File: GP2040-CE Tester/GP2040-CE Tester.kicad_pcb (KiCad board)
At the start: 2 copper layers, 102 x 54 mm, 69 parts, among them J1 USB_B, J2 USB_A, J3 USB_A, U1 RP2040, U2 SIT2018BE-S8-33N-12.000000G, U3 W25Q128JVS, U4 NCP1117-3.3_SOT223, U5 TUSB4041IPAPR, U6 PTMUXHS221NKGR, U7 ATmega2560-16A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

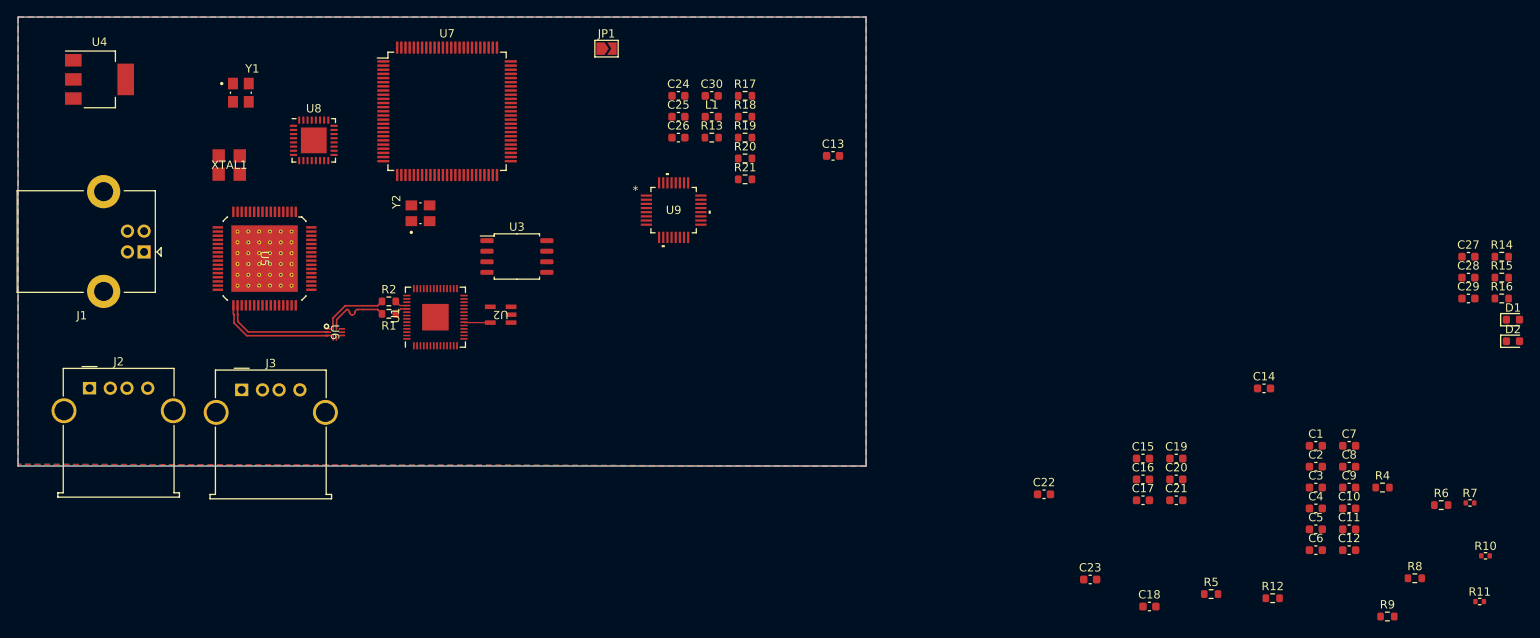
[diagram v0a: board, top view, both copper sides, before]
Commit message: adding most of the components, and schematic connections
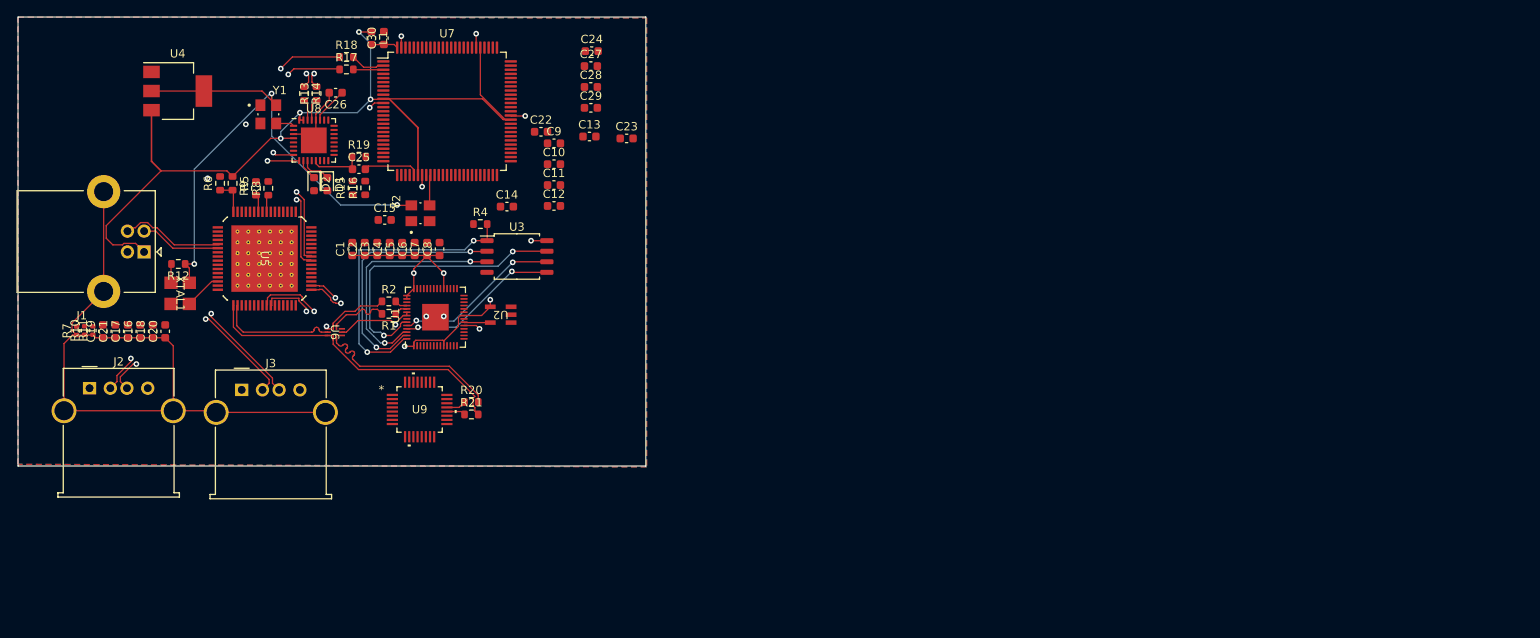
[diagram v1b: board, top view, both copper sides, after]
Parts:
- removed JP1: Jumper_2_Open, Jumper:SolderJumper-2_P1.3mm_Open_TrianglePad1.0x1.5mm
- moved R10 170.7 mm to (99.0, 76.7), turned to 90 degrees
- moved R11 170.0 mm to (100.0, 76.7), turned to 90 degrees
- moved R7 168.9 mm to (98.0, 76.7), turned to 90 degrees
- moved R6 151.9 mm to (115.3, 59.0), turned to 90 degrees
- moved R8 145.7 mm to (121.1, 59.6), turned to 90 degrees
- moved R9 145.5 mm to (119.6, 59.6), turned to 90 degrees
- moved D2 145.4 mm to (126.6, 59.1), turned to -90 degrees
- moved R14 145.4 mm to (125.4, 48.2), turned to -90 degrees
- moved D1 143.5 mm to (128.2, 59.1), turned to -90 degrees
- moved R15 138.6 mm to (131.2, 59.6), turned to 90 degrees
- moved R12 137.6 mm to (110.3, 68.7), turned to 180 degrees
- moved R16 137.3 mm to (132.8, 59.6), turned to 90 degrees
- moved C19 130.0 mm to (101.2, 76.8), turned to 90 degrees
- moved C21 129.2 mm to (102.7, 76.8), turned to 90 degrees
- moved R5 127.6 mm to (116.8, 59.0), turned to -90 degrees
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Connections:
- net /Sheetname: Embeded RP2040/clock renamed /Sheetname: Embeded RP2040/CLK
- net Net-(J1-D+) renamed /Sheetname: USB Hub/UPSD+
- net Net-(J1-D-) renamed /Sheetname: USB Hub/UPSD-
- net Net-(U1-USB_DM) renamed /Sheetname: Embeded RP2040/LD-
- net Net-(U1-USB_DP) renamed /Sheetname: Embeded RP2040/LD+
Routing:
- net +3.3V: track 0.00 -> 164.2 mm, vias 0 -> 9
- net +5V: track 0.00 -> 106.8 mm, vias 0 -> 4
- net Earth: track 0.00 -> 80.6 mm
- net /Sheetname: USB Hub/USB_4_D-: track 0.00 -> 46.6 mm, vias 0 -> 2
- net /Sheetname: USB Hub/USB_4_D+: track 0.00 -> 46.4 mm, vias 0 -> 2
- net /Sheetname: Mega2560/MEGA_USB_D+: track 0.00 -> 38.4 mm, vias 0 -> 2
- net /Sheetname: Mega2560/MEGA_USB_D-: track 0.00 -> 38.4 mm, vias 0 -> 2
- net /Sheetname: USB Hub/USB_3_D+: track 0.00 -> 36.5 mm, vias 0 -> 2
- net /Sheetname: USB Hub/USB_3_D-: track 0.00 -> 36.5 mm, vias 0 -> 2
- net /Sheetname: Embeded RP2040/QSPI_SS: track 0.00 -> 36.0 mm, vias 0 -> 2
- net /Sheetname: Embeded RP2040/QSPI_SD3: track 0.00 -> 34.8 mm, vias 0 -> 2
- net /Sheetname: Embeded RP2040/QSPI_SD1: track 0.00 -> 31.0 mm, vias 0 -> 2
- net /Sheetname: Embeded RP2040/QSPI_SD2: track 0.00 -> 28.3 mm, vias 0 -> 2
- net Net-(U8-PD3): track 0.00 -> 24.4 mm, vias 0 -> 2
- net /Sheetname: Mega2560/SHIELDUSBD-: track 0.00 -> 23.3 mm
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- added copper zone on In1.Cu, net GND
- added copper zone on In2.Cu, net GND
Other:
- board size 102 x 54 mm -> 75.5 x 54 mm
- copper layers 2 -> 4
